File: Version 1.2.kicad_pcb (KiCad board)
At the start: 4 copper layers, 40 x 40 mm, 39 parts, among them J2 Conn_01x02_Pin, J3 Conn_01x12_Socket, J4 Conn_01x16_Socket, J4 Conn_Coaxial, U1 BGA2801, U2 BGA420, U3 AS179-92LF, U4 SX1278, U5 74LVC1G19, Y1 ECS-TXO-2520-33-400-AN-TR

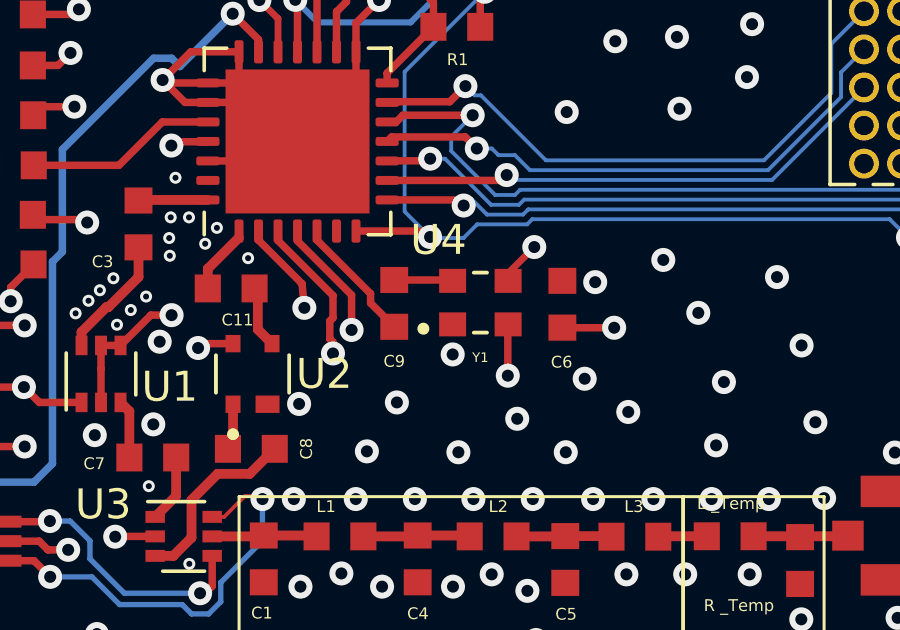
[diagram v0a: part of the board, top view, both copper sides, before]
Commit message: Fix Clock Pads
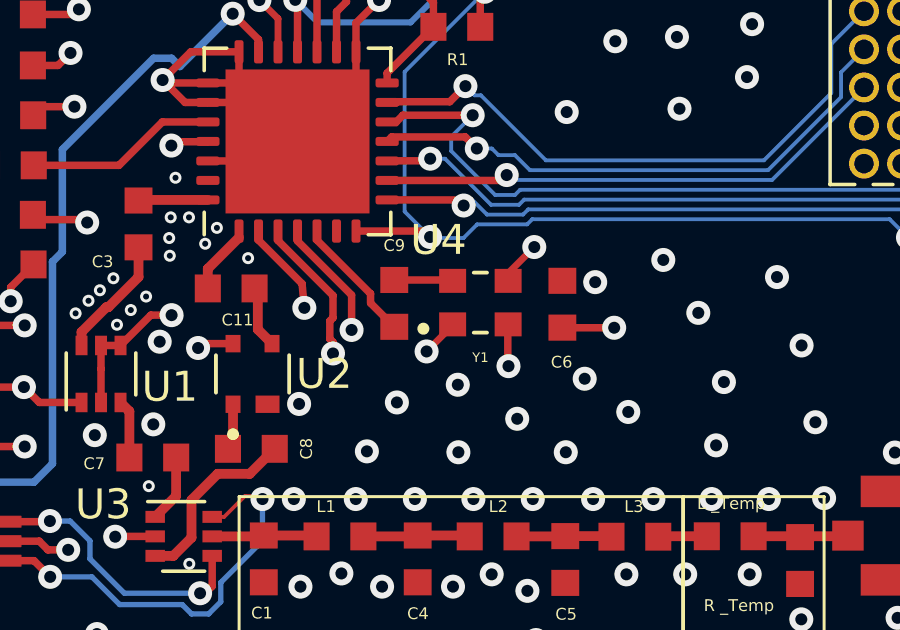
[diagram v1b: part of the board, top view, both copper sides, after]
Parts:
- turned C9 to 90 degrees
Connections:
- U4 pad 5: /TCXO_OUT -> Net-(Y1-VDD)
- Y1 pad 1: GND -> +3.3V
- Y1 pad 2: +3.3V -> GND
- Y1 pad 3: +3.3V -> /TCXO_OUT
- Y1 pad 4: Net-(Y1-VDD) -> +3.3V
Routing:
- net Net-(Y1-VDD): track 1.96 -> 4.26 mm
- net /TCXO_OUT: track 4.26 -> 1.96 mm
- net GND: track 31.2 -> 32.7 mm, vias 116 -> 117
- net +3.3V: track 28.4 -> 27.9 mm
